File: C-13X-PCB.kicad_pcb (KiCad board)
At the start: 2 copper layers, 216.7 x 89.7 mm, 135 parts, among them J1 ai03_Daughterboard_Connector, J2 AVR-TagConnect, SW1 SW_Push, SW2 SW_Push, U1 ATmega32A-AU, U2 SRV05-4, Y1 Crystal_GND24_Small

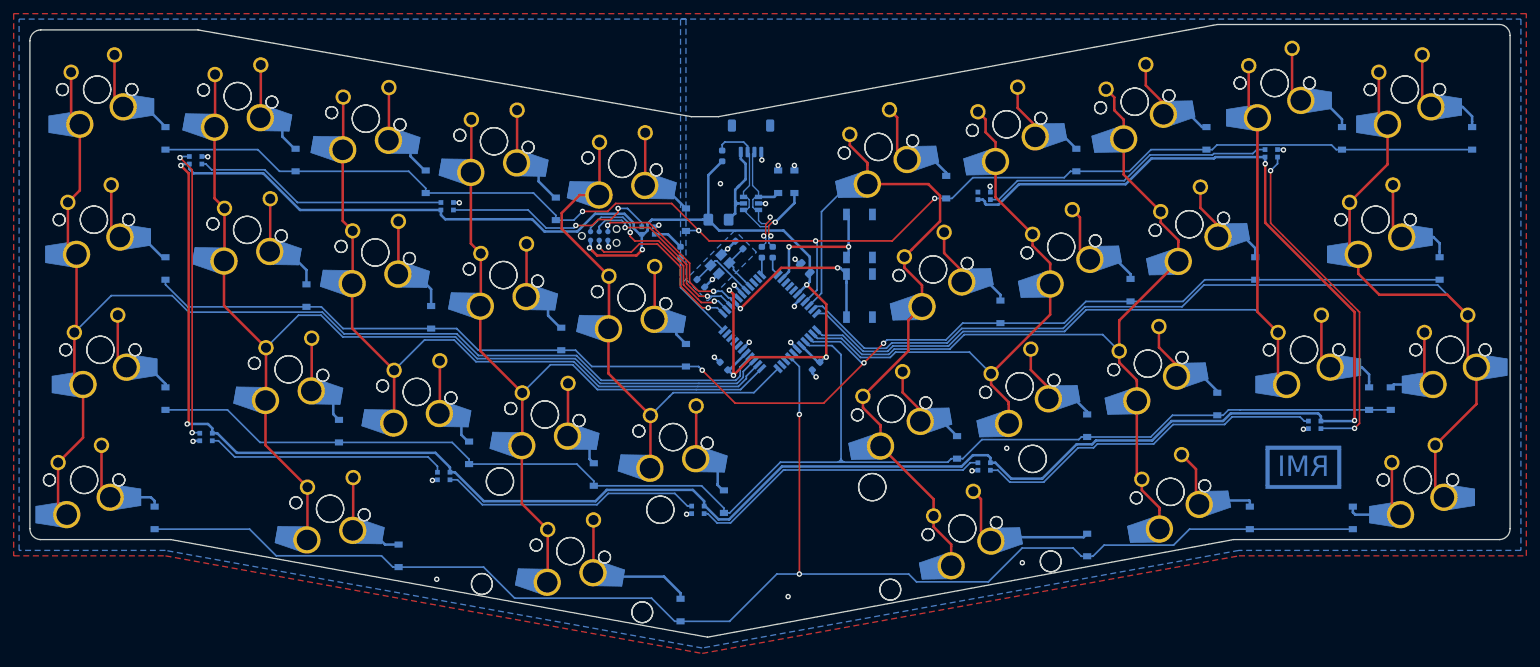
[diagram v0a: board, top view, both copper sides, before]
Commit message: Add LCSC part numbers in BOM, fix RGB
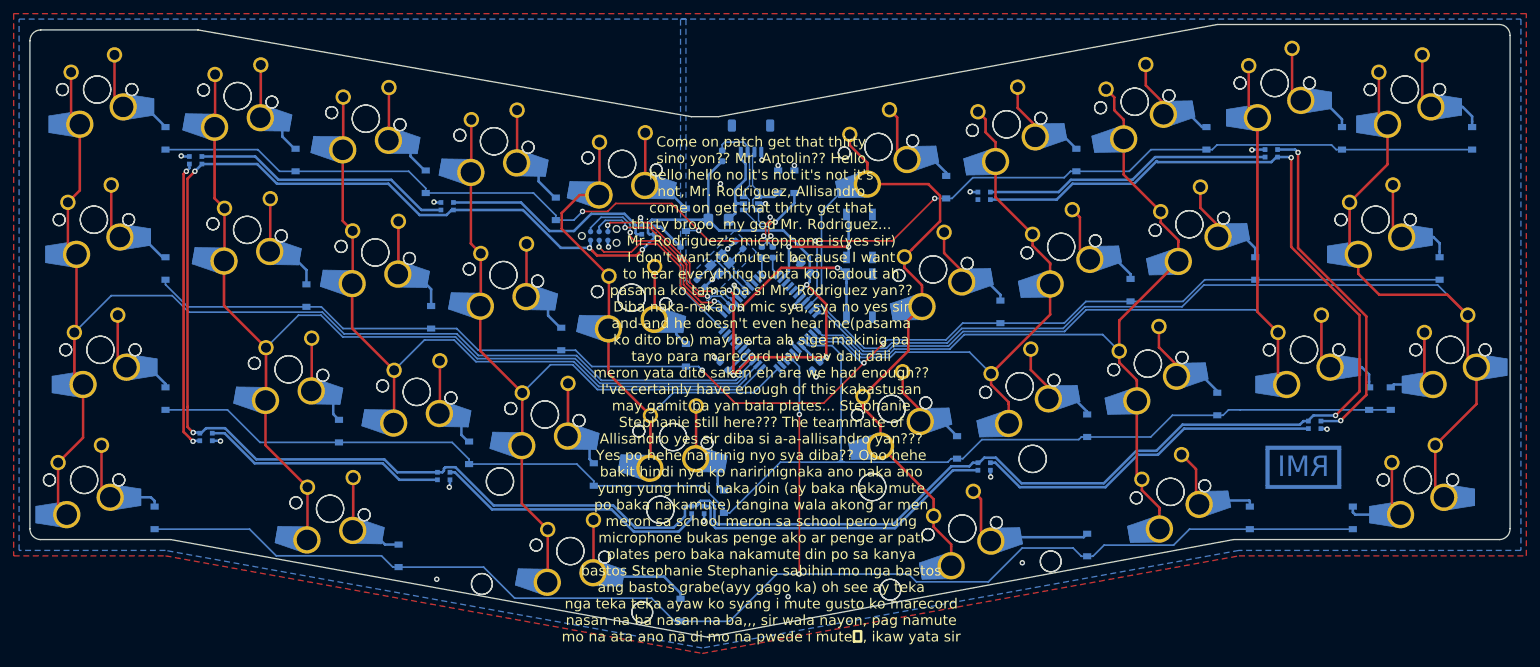
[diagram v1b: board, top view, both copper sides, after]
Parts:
- RGB1, RGB10, RGB2, RGB3, RGB4, RGB5, RGB6, RGB7, RGB8, RGB9: value WS2812B -> WS2812B-2020
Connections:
- RGB1 pad 1: +5V -> Net-(RGB1-Pad1)
- RGB1 pad 2: Net-(RGB1-Pad2) -> GND
- RGB1 pad 3: GND -> /Underglow/RGB
- RGB1 pad 4: /Underglow/RGB -> +5V
- RGB10 pad 1: +5V -> Net-(RGB10-Pad1)
- RGB10 pad 2: Net-(RGB10-Pad2) -> GND
- RGB10 pad 3: GND -> Net-(RGB10-Pad3)
- RGB10 pad 4: Net-(RGB10-Pad4) -> +5V
- RGB2 pad 1: +5V -> Net-(RGB2-Pad1)
- RGB2 pad 2: Net-(RGB2-Pad2) -> GND
- RGB2 pad 3: GND -> Net-(RGB1-Pad1)
- RGB2 pad 4: Net-(RGB1-Pad2) -> +5V
- RGB3 pad 1: +5V -> Net-(RGB3-Pad1)
- RGB3 pad 2: Net-(RGB3-Pad2) -> GND
- RGB3 pad 3: GND -> Net-(RGB2-Pad1)
- RGB3 pad 4: Net-(RGB2-Pad2) -> +5V
- RGB4 pad 1: +5V -> Net-(RGB4-Pad1)
- RGB4 pad 2: Net-(RGB4-Pad2) -> GND
- RGB4 pad 3: GND -> Net-(RGB3-Pad1)
- RGB4 pad 4: Net-(RGB3-Pad2) -> +5V
- RGB5 pad 1: +5V -> Net-(RGB5-Pad1)
- RGB5 pad 2: Net-(RGB5-Pad2) -> GND
- RGB5 pad 3: GND -> Net-(RGB4-Pad1)
- RGB5 pad 4: Net-(RGB4-Pad2) -> +5V
- RGB6 pad 1: +5V -> Net-(RGB6-Pad1)
- RGB6 pad 2: Net-(RGB6-Pad2) -> GND
- RGB6 pad 3: GND -> Net-(RGB5-Pad1)
- RGB6 pad 4: Net-(RGB5-Pad2) -> +5V
- RGB7 pad 1: +5V -> Net-(RGB7-Pad1)
- RGB7 pad 2: Net-(RGB7-Pad2) -> GND
- RGB7 pad 3: GND -> Net-(RGB6-Pad1)
- RGB7 pad 4: Net-(RGB6-Pad2) -> +5V
- RGB8 pad 1: +5V -> Net-(RGB8-Pad1)
- RGB8 pad 2: Net-(RGB8-Pad2) -> GND
- RGB8 pad 3: GND -> Net-(RGB7-Pad1)
- RGB8 pad 4: Net-(RGB7-Pad2) -> +5V
- RGB9 pad 1: +5V -> Net-(RGB10-Pad3)
- RGB9 pad 2: Net-(RGB10-Pad4) -> GND
- RGB9 pad 3: GND -> Net-(RGB8-Pad1)
- RGB9 pad 4: Net-(RGB8-Pad2) -> +5V
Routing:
- net Net-(RGB7-Pad1): track 0.00 -> 51.6 mm
- net Net-(RGB7-Pad2): track 51.5 -> 0.00 mm
- net Net-(RGB8-Pad1): track 0.00 -> 51.0 mm, vias 0 -> 2
- net Net-(RGB8-Pad2): track 50.8 -> 0.00 mm, vias 2 -> 0
- net Net-(RGB6-Pad1): track 0.00 -> 46.3 mm
- net Net-(RGB6-Pad2): track 44.4 -> 0.00 mm
- net Net-(RGB3-Pad2): track 43.6 -> 0.00 mm, vias 2 -> 0
- net Net-(RGB10-Pad4): track 43.2 -> 0.00 mm
- net Net-(RGB3-Pad1): track 0.00 -> 42.5 mm, vias 0 -> 2
- net Net-(RGB10-Pad3): track 0.00 -> 42.3 mm
- net Net-(RGB5-Pad1): track 0.00 -> 40.5 mm
- net Net-(RGB5-Pad2): track 38.3 -> 0.00 mm
- net Net-(RGB2-Pad1): track 0.00 -> 38.2 mm
- net Net-(RGB2-Pad2): track 37.3 -> 0.00 mm
- net Net-(RGB4-Pad1): track 0.00 -> 35.8 mm
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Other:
- board text added: "Come on patch get that thirty sino yon?? Mr. Antolin?? Hello hello hello no it's not it's not it's not, Mr. Rodriguez, Allisandro come on get that thirty get that thirty brooo my god Mr. Rodriguez... Mr. Rodriguez's microphone is(yes sir) I don't want to mute it because I want to hear everything punta ko loadout ah pasama ko tama ba si Mr. Rodriguez yan?? Diba naka-naka on mic sya, sya no yes sir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"
